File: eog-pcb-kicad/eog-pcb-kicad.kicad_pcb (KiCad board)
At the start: 4 copper layers, 92 x 60 mm, 103 parts, among them J1 Conn_01x03, J2 Conn_01x02, J3 Conn_01x02, J4 Conn_01x03, J6 Conn_01x02, U2 AD620, U3 LMC6482, U4 LMC6482, U5 AD620, U6 LMC6482, U7 LMC6482, U8 MAX764ESA+

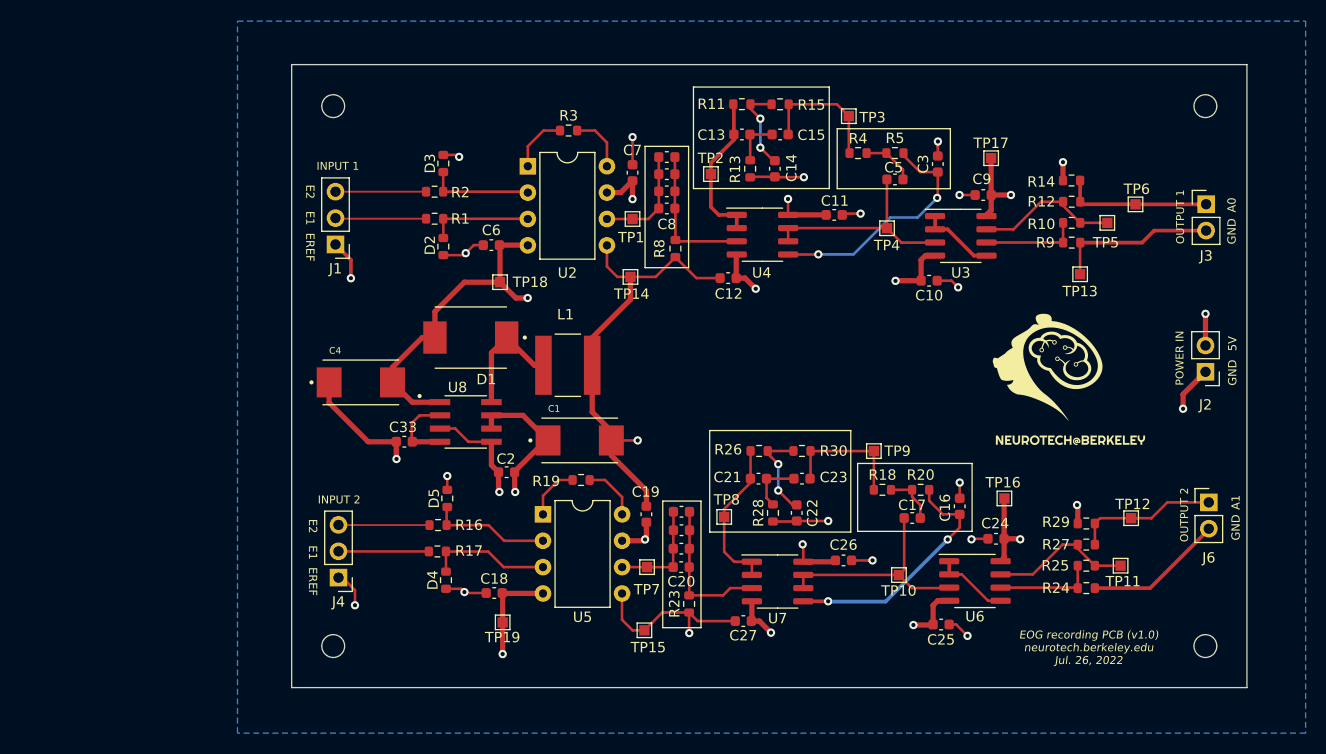
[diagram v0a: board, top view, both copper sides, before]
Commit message: updated the schematics with buffer op-amp and resistor sockets
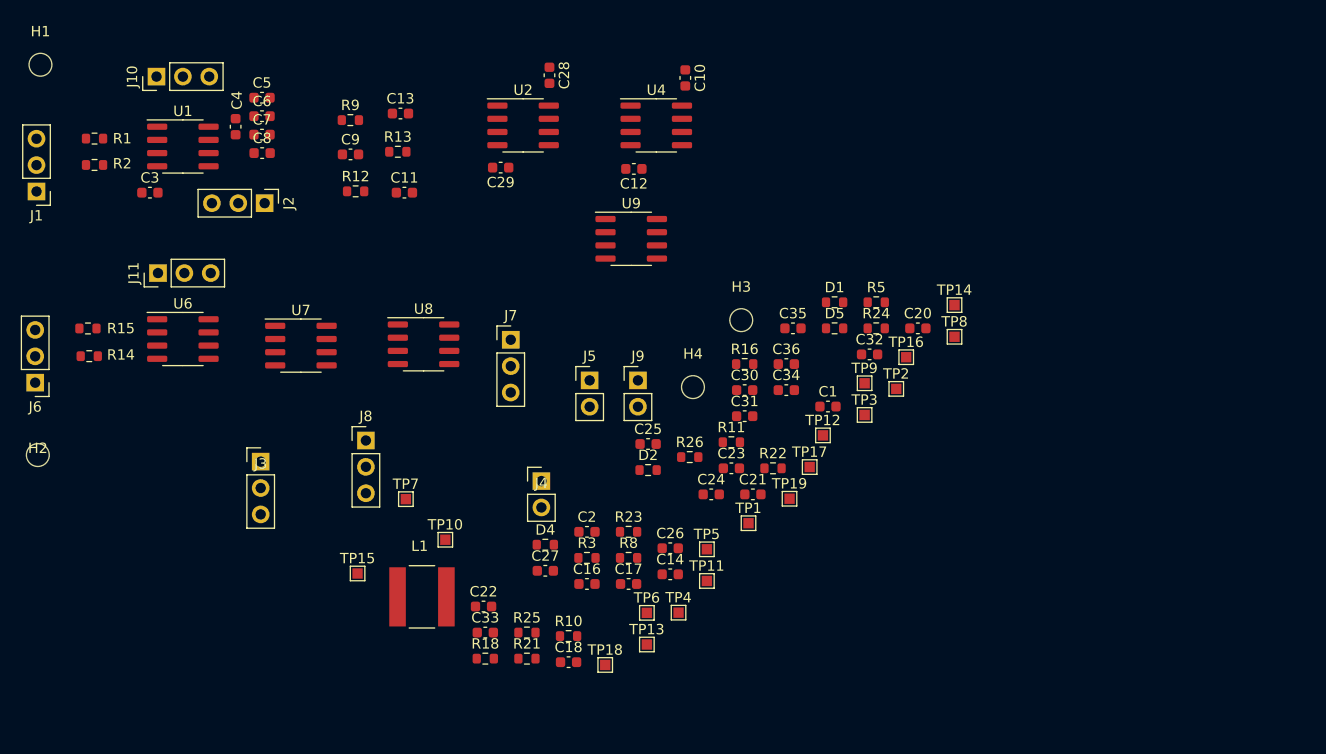
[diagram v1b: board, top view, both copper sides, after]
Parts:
- removed ?, G***: LOGO, LOGO
- removed C15: 1uF, Capacitor_SMD:C_0603_1608Metric
- removed C19: 0.1uF, Capacitor_SMD:C_0603_1608Metric
- removed C201, C202, C203, C81, C82, C83: 10uF, Capacitor_SMD:C_0603_1608Metric
- removed D3: D5V0, Resistor_SMD:R_0603_1608Metric
- removed R17: 220k, Resistor_SMD:R_0603_1608Metric
- removed R19: 2k2, Resistor_SMD:R_0603_1608Metric
- removed R20, R4: 320R, Resistor_SMD:R_0603_1608Metric
- removed R27, R29: 1k, Resistor_SMD:R_0603_1608Metric
- removed R28: 1k3, Resistor_SMD:R_0603_1608Metric
- removed R30: 2k7, Resistor_SMD:R_0603_1608Metric
- removed U3: LMC6482, Package_SO:SOIC-8_3.9x4.9mm_P1.27mm
- removed U5: AD620, Package_DIP:DIP-8_W7.62mm
- added C28: 0.1uF, Capacitor_SMD:C_0603_1608Metric, F.Cu at (120.9, 65.9)
- added C29: 0.1uF, Capacitor_SMD:C_0603_1608Metric, F.Cu at (116.2, 74.8)
- added C30: 1uF, Capacitor_SMD:C_0603_1608Metric, F.Cu at (139.7, 96.2)
- added C31: 0.1uF, Capacitor_SMD:C_0603_1608Metric, F.Cu at (139.7, 98.7)
- added C32: 0.1uF, Capacitor_SMD:C_0603_1608Metric, F.Cu at (151.7, 92.8)
- added C34: 1uF, Capacitor_SMD:C_0603_1608Metric, F.Cu at (143.7, 96.2)
- added C35: 0.1uF, Capacitor_SMD:C_0603_1608Metric, F.Cu at (144.4, 90.3)
- added C36: 0.1uF, Capacitor_SMD:C_0603_1608Metric, F.Cu at (143.7, 93.7)
- added J10: RG0, Connector_PinHeader_2.54mm:PinHeader_1x03_P2.54mm_Vertical, F.Cu at (83.1, 66.0)
- added J11: RG1, Connector_PinHeader_2.54mm:PinHeader_1x03_P2.54mm_Vertical, F.Cu at (83.2, 85.0)
- added J5: Conn_01x02, Connector_PinHeader_2.54mm:PinHeader_1x02_P2.54mm_Vertical, F.Cu at (124.8, 95.3)
- added J7: HPF1, Connector_PinHeader_2.54mm:PinHeader_1x03_P2.54mm_Vertical, F.Cu at (117.2, 91.4)
- added J8: G1, Connector_PinHeader_2.54mm:PinHeader_1x03_P2.54mm_Vertical, F.Cu at (103.2, 101.1)
- added J9: Conn_01x02, Connector_PinHeader_2.54mm:PinHeader_1x02_P2.54mm_Vertical, F.Cu at (129.4, 95.3)
- added R21: 100k, Resistor_SMD:R_0603_1608Metric, F.Cu at (118.7, 122.1)
- added R22: 2k7, Resistor_SMD:R_0603_1608Metric, F.Cu at (142.4, 103.8)
- added U1: AD620, Package_SO:SOIC-8_3.9x4.9mm_P1.27mm, F.Cu at (85.6, 72.8)
- added U9: LMC6482, Package_SO:SOIC-8_3.9x4.9mm_P1.27mm, F.Cu at (128.8, 81.7)
- C1: value 100uF -> 10uF; footprint 20TQC100MYF:CAP_20TQC100MYF -> Capacitor_SMD:C_0603_1608Metric
- C11, C33: value 0.1uF -> 2uF
- C14, C22: value 2uF -> 0.1uF
- C16, C17, C3: value 10uF -> 0.1uF
- C2, C24, C25, C26, C27, C6, C7: value 0.1uF -> 10uF
- C21: value 1uF -> 10uF
- C23: value 1uF -> 0.1uF
- C4: value 68uF -> 0.1uF; footprint 20TQC100MYF:CAP_20TQC100MYF -> Capacitor_SMD:C_0603_1608Metric
- C9: value 0.1uF -> 1uF
- D1: value MBRS330T3G -> D5V0; footprint MBRS330T3G:DIOM7959X261N -> Resistor_SMD:R_0603_1608Metric
- J1: value Conn_01x03 -> INPUT0
- J2: value Conn_01x02 -> HPF0; footprint Connector_PinHeader_2.54mm:PinHeader_1x02_P2.54mm_Vertical -> Connector_PinHeader_2.54mm:PinHeader_1x03_P2.54mm_Vertical
- J3: value Conn_01x02 -> G0; footprint Connector_PinHeader_2.54mm:PinHeader_1x02_P2.54mm_Vertical -> Connector_PinHeader_2.54mm:PinHeader_1x03_P2.54mm_Vertical
- J4: value Conn_01x03 -> Conn_01x02; footprint Connector_PinHeader_2.54mm:PinHeader_1x03_P2.54mm_Vertical -> Connector_PinHeader_2.54mm:PinHeader_1x02_P2.54mm_Vertical
- J6: value Conn_01x02 -> INPUT1; footprint Connector_PinHeader_2.54mm:PinHeader_1x02_P2.54mm_Vertical -> Connector_PinHeader_2.54mm:PinHeader_1x03_P2.54mm_Vertical
- R10: value 100k -> 1k
- R11: value 2k7 -> 1k
- R12: value 1k -> 1k3
- R13: value 1k3 -> 2k7
- R14: value 1k -> 220k
- R15: value 2k7 -> 220k
- R16: value 220k -> 320R
- R23: value 10k -> 1k
- R24: value 150R -> 1k
- R25: value 100k -> 1k3
- R3: value 2k2 -> 320R
- R8: value 10k -> 100k
- R9: value 150R -> 2k7
- U2: value AD620 -> LMC6482; footprint Package_DIP:DIP-8_W7.62mm -> Package_SO:SOIC-8_3.9x4.9mm_P1.27mm
- U6: value LMC6482 -> AD620
- U8: value MAX764ESA+ -> LMC6482; footprint MAX764ESA_:SOIC127P600X175-8N -> Package_SO:SOIC-8_3.9x4.9mm_P1.27mm
- moved H2 117.4 mm to (71.6, 102.5)
- moved J6 113.6 mm to (71.4, 95.5), turned to 180 degrees
- moved R14 96.1 mm to (76.6, 93.0), turned to 0 degrees
- moved J3 94.4 mm to (93.1, 103.1)
- moved J2 92.1 mm to (93.5, 78.2), turned to -90 degrees
- moved U6 79.8 mm to (85.6, 91.3)
- moved C3 75.9 mm to (82.4, 77.2), turned to 0 degrees
- moved R9 70.5 mm to (101.7, 70.2), turned to 0 degrees
- moved R15 70.1 mm to (76.5, 90.3), turned to 0 degrees
- moved R12 69.0 mm to (102.2, 77.1), turned to 0 degrees
- moved R10 62.7 mm to (122.7, 119.9), turned to 0 degrees
- moved C5 61.5 mm to (93.2, 68.1), turned to 0 degrees
- moved TP6 61.3 mm to (130.3, 117.7)
- moved C9 61.1 mm to (101.7, 73.5)
- moved TP13 54.9 mm to (130.3, 120.7)
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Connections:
- C1 pad 1: VDD -> GND
- C1 pad 2: GND -> /LPF_IN+_CH0
- C10 pad 2: VDD_NEG_5V -> VDD
- C11 pad 2: VDD -> Net-(C11-Pad2)
- C13 pad 1: /NOTCH_IN_CH0 -> Net-(C13-Pad1)
- C13 pad 2: Net-(C13-Pad2) -> NOTCH_OUT_CH0
- C14 pad 2: Net-(C14-Pad2) -> VDD
- C16 pad 2: /LPF_IN+_CH1 -> VDD_NEG_5V
- C17 pad 1: Net-(C17-Pad1) -> VDD
- C17 pad 2: /LPF_OUT_CH1 -> GND
- C18 pad 1: GND -> /FB/REF
- C18 pad 2: VDD_NEG_5V -> GND
- C2 pad 1: VDD -> Net-(C2-Pad1)
- C2 pad 2: GND -> /LPF_IN-_CH0
- C20 pad 1: /IA_OUT_CH1 -> GND
- C20 pad 2: /HPF_OUT_CH1 -> /LPF_IN+_CH1
- C21 pad 1: /NOTCH_IN_CH1 -> Net-(C21-Pad1)
- C21 pad 2: Net-(C21-Pad2) -> /LPF_IN-_CH1
- C22 pad 2: Net-(C22-Pad2) -> VDD_NEG_5V
- C23 pad 1: Net-(C21-Pad2) -> GND
- C23 pad 2: NOTCH_OUT_CH1 -> VDD
- C24 pad 1: GND -> /IA_OUT_CH1
- C24 pad 2: VDD -> /HPF_OUT_CH1
- C25 pad 1: GND -> /IA_OUT_CH1
- C25 pad 2: VDD_NEG_5V -> /HPF_OUT_CH1
- C26 pad 1: GND -> /IA_OUT_CH1
- C26 pad 2: VDD -> /HPF_OUT_CH1
- C27 pad 1: GND -> /IA_OUT_CH1
- C27 pad 2: VDD_NEG_5V -> /HPF_OUT_CH1
- C3 pad 2: /LPF_IN+_CH0 -> VDD_NEG_5V
- C33 pad 1: /FB/REF -> GND
- C33 pad 2: GND -> Net-(C33-Pad2)
- C4 pad 2: VDD_NEG_5V -> VDD
- C5 pad 1: Net-(C5-Pad1) -> /IA_OUT_CH0
- C5 pad 2: /LPF_OUT_CH0 -> /HPF_OUT_CH0
- C6 pad 1: GND -> /IA_OUT_CH0
- C6 pad 2: VDD_NEG_5V -> /HPF_OUT_CH0
- C7 pad 1: GND -> /IA_OUT_CH0
- C7 pad 2: VDD -> /HPF_OUT_CH0
- C9 pad 1: GND -> /NOTCH_IN_CH0
- C9 pad 2: VDD -> Net-(C13-Pad1)
- D4 pad 2: /IA_IN+_CH1 -> /IA_IN-_CH1
- D5 pad 2: /IA_IN-_CH1 -> /IA_IN+_CH1
- J2 pad 1: GND -> /HPF_OUT_CH0
- J2 pad 2: VDD -> unconnected-(J2-Pad2)
- J3 pad 1: /AOUT_CH0 -> /AMP_IN-_CH0
- J3 pad 2: GND -> unconnected-(J3-Pad2)
- J4 pad 2: E1_CH1 -> VDD
- J6 pad 1: /AOUT_CH1 -> GND
- J6 pad 2: GND -> E1_CH1
- R1 pad 1: E1_CH0 -> E2_CH0
- R1 pad 2: /IA_IN+_CH0 -> /IA_IN-_CH0
- R10 pad 1: /AMP_OUT_CH0 -> /AOUT_CH0
- R10 pad 2: /AMP_IN-_CH0 -> /AMP_OUT_CH0
- R11 pad 1: Net-(C14-Pad2) -> /AOUT_CH0
- R11 pad 2: /NOTCH_IN_CH0 -> VDD
- R12 pad 1: /AOUT_CH0 -> Net-(C13-Pad1)
- R12 pad 2: /AMP_OUT_CH0 -> GND
- R13 pad 1: Net-(C13-Pad2) -> NOTCH_OUT_CH0
- R13 pad 2: GND -> Net-(C11-Pad2)
- R14 pad 1: /AOUT_CH0 -> E1_CH1
- R14 pad 2: VDD -> /IA_IN+_CH1
- R15 pad 1: NOTCH_OUT_CH0 -> E2_CH1
- R15 pad 2: Net-(C14-Pad2) -> /IA_IN-_CH1
- R16 pad 1: E2_CH1 -> /BUFF1_OUT
- R16 pad 2: /IA_IN-_CH1 -> Net-(C21-Pad1)
- R18 pad 1: NOTCH_OUT_CH1 -> Net-(C21-Pad1)
- R18 pad 2: Net-(C17-Pad1) -> /LPF_IN+_CH1
- R2 pad 1: E2_CH0 -> E1_CH0
- R2 pad 2: /IA_IN-_CH0 -> /IA_IN+_CH0
- R23 pad 1: GND -> /AOUT_CH1
- R23 pad 2: /HPF_OUT_CH1 -> /AMP_OUT_CH1
- R24 pad 1: GND -> /AOUT_CH1
- R24 pad 2: /AMP_IN-_CH1 -> VDD
- R25 pad 1: /AMP_OUT_CH1 -> Net-(C30-Pad2)
- R25 pad 2: /AMP_IN-_CH1 -> GND
- R26 pad 1: Net-(C22-Pad2) -> NOTCH_OUT_CH1
- R26 pad 2: /NOTCH_IN_CH1 -> Net-(C33-Pad2)
- R3 pad 1: Net-(R3-Pad1) -> /BUFF0_OUT
- R3 pad 2: Net-(R3-Pad2) -> Net-(C2-Pad1)
- R5 pad 1: Net-(C5-Pad1) -> Net-(C2-Pad1)
- R8 pad 1: GND -> /AMP_OUT_CH0
- R8 pad 2: /HPF_OUT_CH0 -> /AMP_IN-_CH0
- R9 pad 1: GND -> Net-(C11-Pad2)
- R9 pad 2: /AMP_IN-_CH0 -> /NOTCH_IN_CH0
- TP10 pad 1: /LPF_OUT_CH1 -> VDD_NEG_5V
- TP11 pad 1: /AMP_OUT_CH1 -> VDD_NEG_5V
- TP12 pad 1: /AOUT_CH1 -> /AOUT_CH0
- TP13 pad 1: GND -> NOTCH_OUT_CH0
- TP14 pad 1: GND -> /IA_OUT_CH1
- TP15 pad 1: GND -> /LPF_IN-_CH1
- TP16 pad 1: VDD -> /NOTCH_IN_CH1
- TP17 pad 1: VDD -> /AMP_OUT_CH1
- TP18 pad 1: VDD_NEG_5V -> /AOUT_CH1
- TP19 pad 1: VDD_NEG_5V -> NOTCH_OUT_CH1
- TP2 pad 1: /NOTCH_IN_CH0 -> /LPF_IN-_CH0
- TP3 pad 1: NOTCH_OUT_CH0 -> /NOTCH_IN_CH0
- TP4 pad 1: /LPF_OUT_CH0 -> GND
- TP5 pad 1: /AMP_OUT_CH0 -> GND
- TP6 pad 1: /AOUT_CH0 -> GND
- TP7 pad 1: /IA_OUT_CH1 -> /AMP_OUT_CH0
- TP8 pad 1: /NOTCH_IN_CH1 -> VDD
- TP9 pad 1: NOTCH_OUT_CH1 -> VDD
- U2 pad 1: Net-(R3-Pad1) -> /NOTCH_IN_CH0
- U2 pad 2: /IA_IN-_CH0 -> /NOTCH_IN_CH0
- U2 pad 3: /IA_IN+_CH0 -> /HPF_OUT_CH0
- U2 pad 5: GND -> NOTCH_OUT_CH0
- U2 pad 6: /IA_OUT_CH0 -> /BUFF0_OUT
- U2 pad 7: VDD -> /BUFF0_OUT
- U2 pad 8: Net-(R3-Pad2) -> VDD
- U4 pad 1: /NOTCH_IN_CH0 -> /LPF_IN-_CH0
- U4 pad 2: /NOTCH_IN_CH0 -> /LPF_IN-_CH0
- U4 pad 3: /HPF_OUT_CH0 -> /LPF_IN+_CH0
- U4 pad 5: /LPF_IN+_CH0 -> /LPF_IN-_CH0
- U4 pad 6: /LPF_OUT_CH0 -> /AMP_IN+_CH0
- U4 pad 7: /LPF_OUT_CH0 -> /AMP_IN+_CH0
- U6 pad 1: /AMP_IN+_CH1 -> RG10
- U6 pad 2: /AMP_IN+_CH1 -> /IA_IN-_CH1
- U6 pad 3: /LPF_OUT_CH1 -> /IA_IN+_CH1
- U6 pad 5: /AMP_IN+_CH1 -> GND
- U6 pad 6: /AMP_IN-_CH1 -> /IA_OUT_CH1
- U6 pad 7: /AMP_OUT_CH1 -> VDD
- U6 pad 8: VDD -> RG11
- U7 pad 5: /LPF_IN+_CH1 -> NOTCH_OUT_CH1
- U7 pad 6: /LPF_OUT_CH1 -> /BUFF1_OUT
- U7 pad 7: /LPF_OUT_CH1 -> /BUFF1_OUT
- U8 pad 1: VDD_NEG_5V -> /LPF_IN-_CH1
- U8 pad 2: /FB/REF -> /LPF_IN-_CH1
- U8 pad 3: GND -> /LPF_IN+_CH1
- U8 pad 4: /FB/REF -> VDD_NEG_5V
- U8 pad 5: GND -> /LPF_IN-_CH1
- U8 pad 6: VDD -> /AMP_IN+_CH1
- U8 pad 7: VDD -> /AMP_IN+_CH1
- U8 pad 8: /LX -> VDD
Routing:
- net GND: track 162.2 -> 0.00 mm, vias 22 -> 0
- net VDD_NEG_5V: track 61.5 -> 0.00 mm, vias 6 -> 0
- net VDD: track 55.0 -> 0.00 mm, vias 10 -> 0
- net /LPF_IN+_CH1: track 23.8 -> 0.00 mm, vias 2 -> 0
- net /LPF_IN+_CH0: track 23.3 -> 0.00 mm, vias 2 -> 0
- net /LPF_OUT_CH1: track 21.6 -> 0.00 mm
- net /LPF_OUT_CH0: track 20.7 -> 0.00 mm
- net /NOTCH_IN_CH1: track 15.1 -> 0.00 mm
- net /NOTCH_IN_CH0: track 14.6 -> 0.00 mm
- net /HPF_OUT_CH1: track 14.4 -> 0.00 mm
- net /AOUT_CH0: track 14.0 -> 0.00 mm
- net /HPF_OUT_CH0: track 14.0 -> 0.00 mm
- net /AOUT_CH1: track 13.9 -> 0.00 mm
- net /AMP_OUT_CH1: track 13.8 -> 0.00 mm
- net /AMP_OUT_CH0: track 13.8 -> 0.00 mm
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- removed copper zone on In1.Cu, net GND
- removed copper zone on In2.Cu, net VDD
- removed copper zone on B.Cu, net VDD_NEG_5V
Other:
- board outline removed
- copper layers 4 -> 2
- board text removed: "5V"
- board text removed: "A0"
- board text removed: "A1"
- board text removed: "E1"
- board text removed: "E2"
- board text removed: "EOG recording PCB (v1.0) neurotech.berkeley.edu Jul. 26, 2022"
- board text removed: "EREF"
- board text removed: "GND"
- board text removed: "INPUT 1"
- board text removed: "INPUT 2"
- board text removed: "OUTPUT 1"
- board text removed: "OUTPUT 2"
- board text removed: "POWER IN"

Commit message: preliminary layout and added libraries
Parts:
- removed TP12, TP18: TestPoint, TestPoint:TestPoint_Pad_1.0x1.0mm
- added C15: 100uF, 20TQC100MYF:CAP_20TQC100MYF, F.Cu at (126.2, 101.9)
- added C19: 68uF, 20TQC100MYF:CAP_20TQC100MYF, F.Cu at (81.2, 80.1)
- added D3: MBRS330T3G, MBRS330T3G:DIOM7959X261N, F.Cu at (86.3, 87.4)
- added U5: MAX764ESA+, MAX764ESA_:SOIC127P600X175-8N, F.Cu at (76.4, 87.2)
- J5: value Conn_01x02 -> OUT0
- J9: value Conn_01x02 -> OUT1
- moved D5 74.0 mm to (75.2, 101.6)
- moved D1 73.4 mm to (77.1, 70.4)
- moved TP14 68.0 mm to (92.2, 93.9)
- moved TP1 64.1 mm to (92.7, 65.9)
- moved C18 61.6 mm to (71.4, 88.4), turned to 90 degrees
- moved D2 60.1 mm to (77.1, 76.2)
- moved TP3 58.0 mm to (99.1, 73.4)
- moved TP16 56.6 mm to (99.1, 99.4)
- moved C23 48.7 mm to (89.9, 99.8), turned to -90 degrees
- moved D4 48.0 mm to (75.1, 95.6)
- moved TP2 47.7 mm to (111.6, 74.8)
- moved C20 47.6 mm to (111.9, 107.1), turned to 90 degrees
- moved C24 44.7 mm to (92.7, 97.0)
- moved R22 44.2 mm to (99.1, 95.5), turned to 180 degrees
- moved R5 42.5 mm to (110.9, 78.5)
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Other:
- board outline added: 72.6 x 50 mm

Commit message: layout is 90 percent done
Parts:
- added G***: LOGO, LOGO, F.Cu at (48.0, 4.95)
- moved TP4 193.3 mm to (10.4, 4.57)
- moved TP13 163.2 mm to (36.7, 18.0)
- moved TP6 148.5 mm to (34.9, 46.5)
- moved TP5 141.2 mm to (52.2, 34.3)
- moved TP11 138.0 mm to (50.9, 46.5)
- moved TP17 131.8 mm to (46.0, 25.3)
- moved TP19 128.7 mm to (38.5, 46.5)
- moved C17 109.6 mm to (43.7, 30.0)
- moved C32 106.9 mm to (34.7, 27.7), turned to 0 degrees
- moved C15 105.3 mm to (46.2, 33.4)
- moved U9 102.1 mm to (40.3, 25.8)
- moved C31 101.2 mm to (43.2, 22.1), turned to 180 degrees
- moved J8 98.8 mm to (52.7, 27.7), turned to 90 degrees
- moved H4 93.8 mm to (66.5, 3.50)
- moved C11 93.7 mm to (36.4, 4.32)
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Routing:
- net GND: track 0.00 -> 195.7 mm, vias 0 -> 15
- net VDD: track 0.00 -> 46.1 mm, vias 0 -> 8
- net VDD_NEG_5V: track 0.00 -> 33.8 mm
- net /AMP_IN+_CH1: track 0.00 -> 28.4 mm
- net /AMP_IN+_CH0: track 0.00 -> 25.7 mm, vias 0 -> 2
- net /AMP_IN-_CH0: track 0.00 -> 25.2 mm, vias 0 -> 2
- net /AMP_OUT_CH0: track 0.00 -> 24.1 mm, vias 0 -> 2
- net /AMP_OUT_CH1: track 0.00 -> 20.4 mm
- net NOTCH_OUT_CH0: track 0.00 -> 20.1 mm
- net /AMP_IN-_CH1: track 0.00 -> 20.0 mm, vias 0 -> 2
- net NOTCH_OUT_CH1: track 0.00 -> 19.7 mm
- net /LX: track 0.00 -> 19.2 mm
- net /HPF_OUT_CH1: track 0.00 -> 16.0 mm
- net /HPF_OUT_CH0: track 0.00 -> 15.4 mm
- net /IA_OUT_CH1: track 0.00 -> 13.5 mm
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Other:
- board size 72.6 x 50 mm -> 70 x 50 mm
- copper layers 2 -> 4
- board text added: "-5V"
- board text added: "E+"
- board text added: "E-"
- board text added: "GAIN0"
- board text added: "GAIN1"
- board text added: "GND"
- board text added: "HPF0"
- board text added: "Neurotech @ Berkeley"
- board text added: "OUT_0"
- board text added: "OUT_1"
- board text added: "REF"
- board text added: "RG0"
- board text added: "RG1"
- board text added: "RG10"
- board text added: "RG11"
- board text added: "VDD"
